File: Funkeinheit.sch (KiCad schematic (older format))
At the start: 41 parts, among them Q3 MMBT5551-TP, Q4 MMBT5551-TP, Q5 MMBT5551-TP, Q6 MMBT5551-TP, Q7 MMBT5551-TP, Q8 MMBT5551-TP, U4 LTC3113, U5 RFM23BP

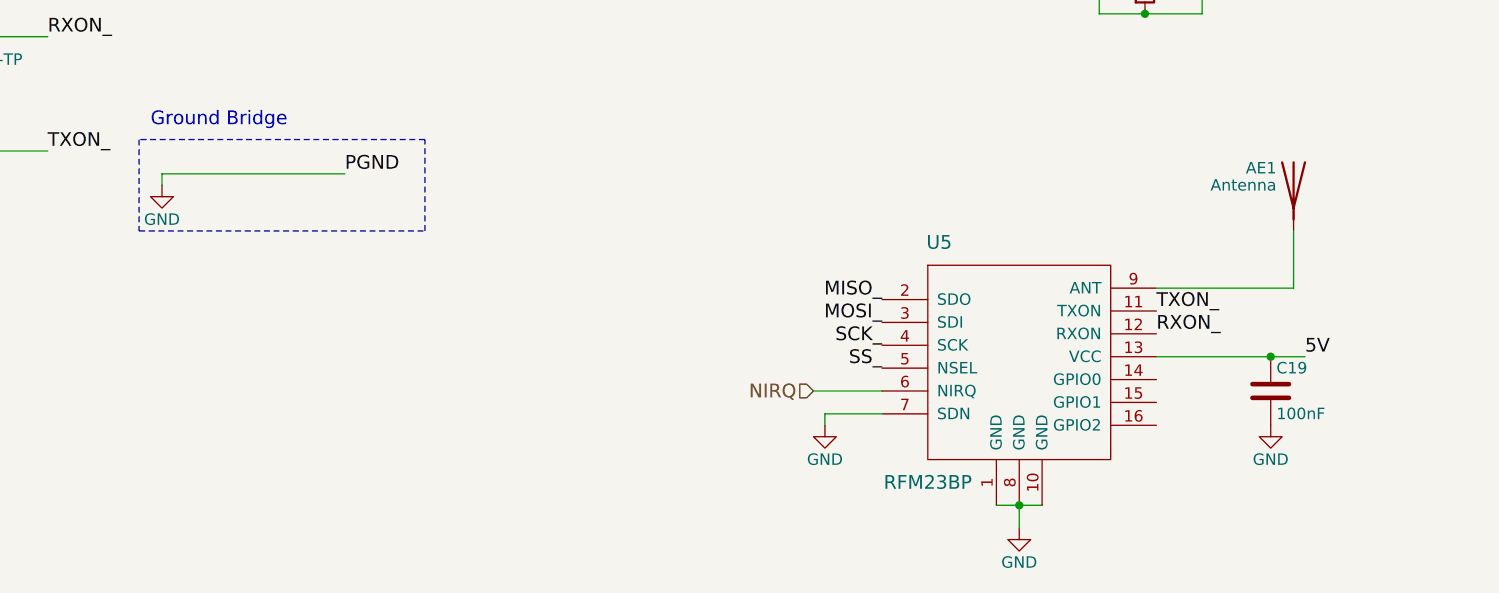
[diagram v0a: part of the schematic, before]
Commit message: Adds RFM23BP Footprint and places module on board
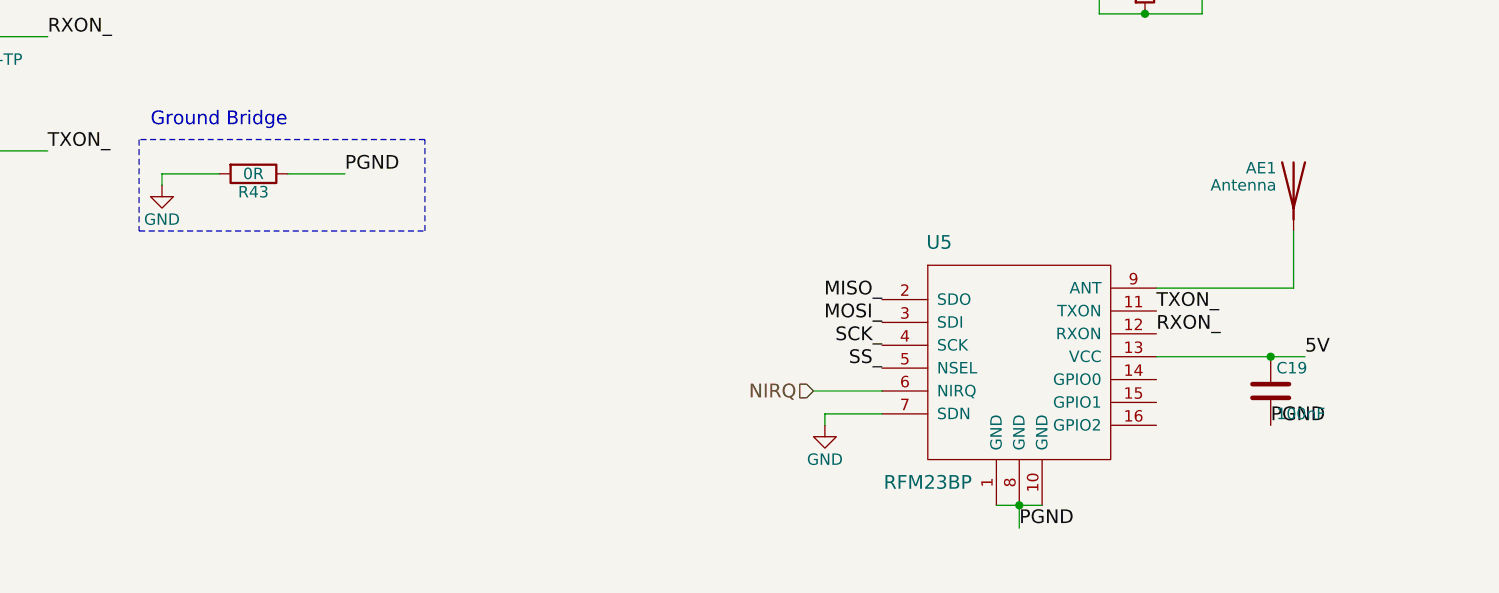
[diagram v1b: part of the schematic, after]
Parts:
- added R43: 0R, Resistors_SMD:R_0603_HandSoldering, symbol R
- C16: footprint Capacitors_SMD:C_1210_HandSoldering -> Capacitors_SMD:C_0603_HandSoldering
- U5: footprint (none) -> HopeRF:RFM23BP
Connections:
- net GND: now also R43.2; no longer C13.2, C14.2, C15.2, C19.2, U4.1 (PGND), U4.10 (PGND), U4.11 (PGND), U4.20 (PGND), U4.21 (PAD), U5.1 (GND), U5.10 (GND), U5.8 (GND)
- new net PGND: C13.2, C14.2, C15.2, C19.2, R43.1, U4.1 (PGND), U4.10 (PGND), U4.11 (PGND), U4.20 (PGND), U4.21 (PAD), U5.1 (GND), U5.10 (GND), U5.8 (GND)
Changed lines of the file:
@@
 Wire Wire Line
 	4750 3700 4750 3650
-Wire Wire Line
-	4750 3650 5550 3650
 Text Label 5550 3650 0    60   ~ 0
 PGND
@@
 F 0 "C16" H 9075 2200 50  0000 L CNN
 F 1 "47pF" H 9075 2000 50  0000 L CNN
-F 2 "Capacitors_SMD:C_1210_HandSoldering" H 9088 1950 50  0001 C CNN
+F 2 "Capacitors_SMD:C_0603_HandSoldering" H 9088 1950 50  0001 C CNN
 F 3 "" H 9050 2100 50  0001 C CNN
 	1    9050 2100
@@
 F 0 "U5" H 8150 5050 60  0000 C CNN
 F 1 "RFM23BP" H 8100 4000 60  0000 C CNN
-F 2 "" H 9000 3800 60  0001 C CNN
+F 2 "HopeRF:RFM23BP" H 9000 3800 60  0001 C CNN
 F 3 "" H 9000 3800 60  0001 C CNN
 	1    8500 4500
@@
 Wire Wire Line
 	9700 4150 9700 3900
-$Comp
-L GND #PWR035
-U 1 1 59C98D82
-P 8500 5200
-F 0 "#PWR035" H 8500 4950 50  0001 C CNN
-F 1 "GND" H 8500 5050 50  0000 C CNN
-F 2 "" H 8500 5200 50  0001 C CNN
-F 3 "" H 8500 5200 50  0001 C CNN
-	1    8500 5200
-	1    0    0    -1
-$EndComp
 Wire Wire Line
 	8400 5100 8600 5100
@@
 Connection ~ 8500 5100
 $Comp
-L GND #PWR036
+L GND #PWR035
 U 1 1 59C9947D
 P 7650 4750
-F 0 "#PWR036" H 7650 4500 50  0001 C CNN
+F 0 "#PWR035" H 7650 4500 50  0001 C CNN
 F 1 "GND" H 7650 4600 50  0000 C CNN
 F 2 "" H 7650 4750 50  0001 C CNN
@@
 F 3 "" H 9600 4600 50  0001 C CNN
 	1    9600 4600
-	1    0    0    -1
-$EndComp
-$Comp
-L GND #PWR037
-U 1 1 59CB2BA8
-P 9600 4750
-F 0 "#PWR037" H 9600 4500 50  0001 C CNN
-F 1 "GND" H 9600 4600 50  0000 C CNN
-F 2 "" H 9600 4750 50  0001 C CNN
-F 3 "" H 9600 4750 50  0001 C CNN
-	1    9600 4750
 	1    0    0    -1
 $EndComp
@@
 Text Label 9100 4350 0    60   ~ 0
 RXON_
+$Comp
+L R R43
+U 1 1 59DBF7EA
+P 5150 3650
+F 0 "R43" V 5230 3650 50  0000 C CNN
+F 1 "0R" V 5150 3650 50  0000 C CNN
+F 2 "Resistors_SMD:R_0603_HandSoldering" V 5080 3650 50  0001 C CNN
+F 3 "" H 5150 3650 50  0001 C CNN
+	1    5150 3650
+	0    1    1    0
+$EndComp
+Wire Wire Line
+	4750 3650 5000 3650
+Wire Wire Line
+	5300 3650 5550 3650
+Text Label 8500 5200 0    60   ~ 0
+PGND
+Text Label 9600 4750 0    60   ~ 0
+PGND
 $EndSCHEMATC

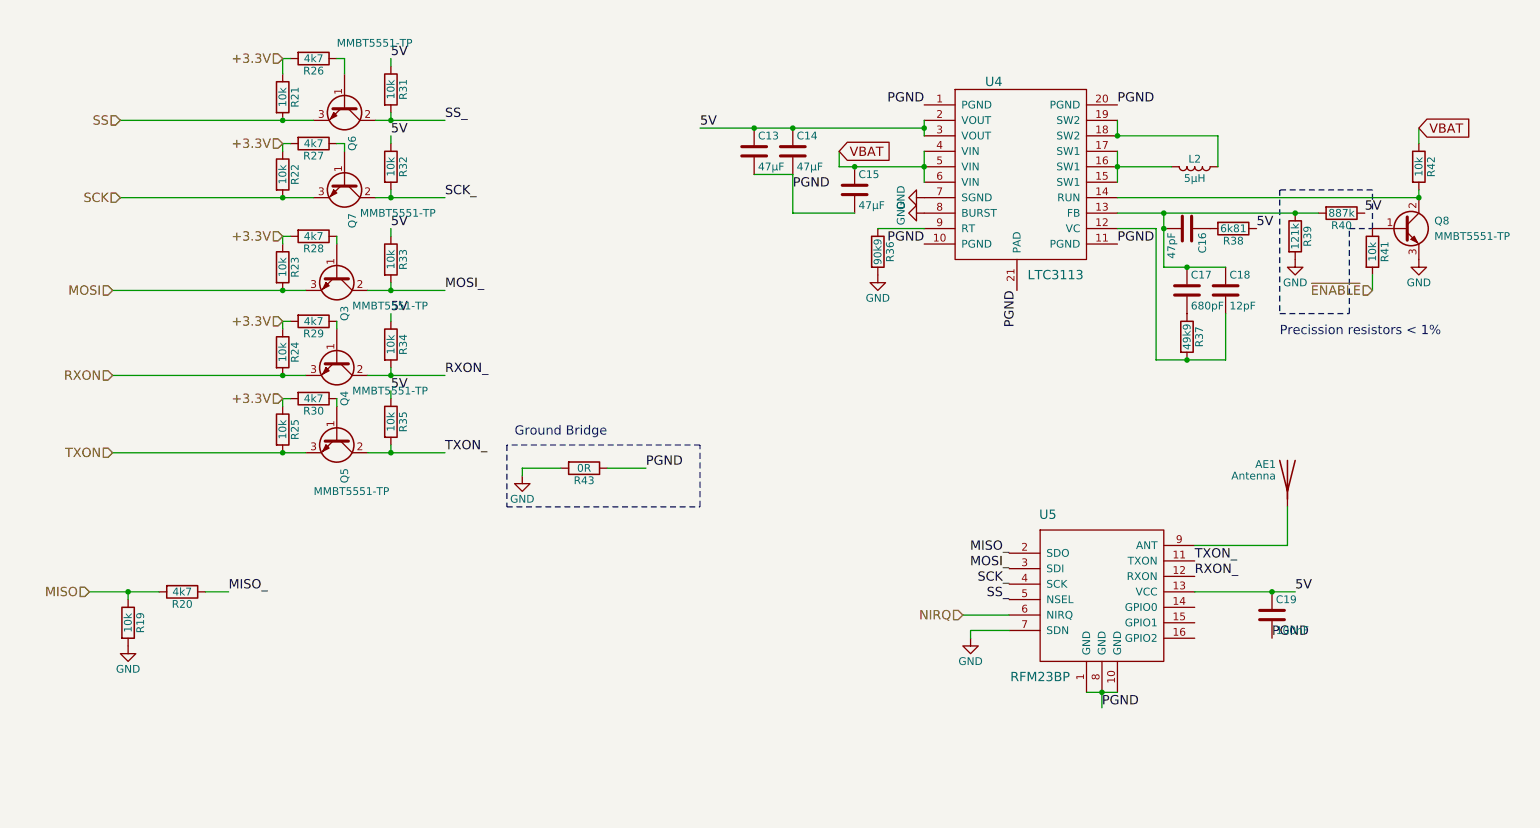
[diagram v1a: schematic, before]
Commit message: Adds Levelshifter for NIRQ
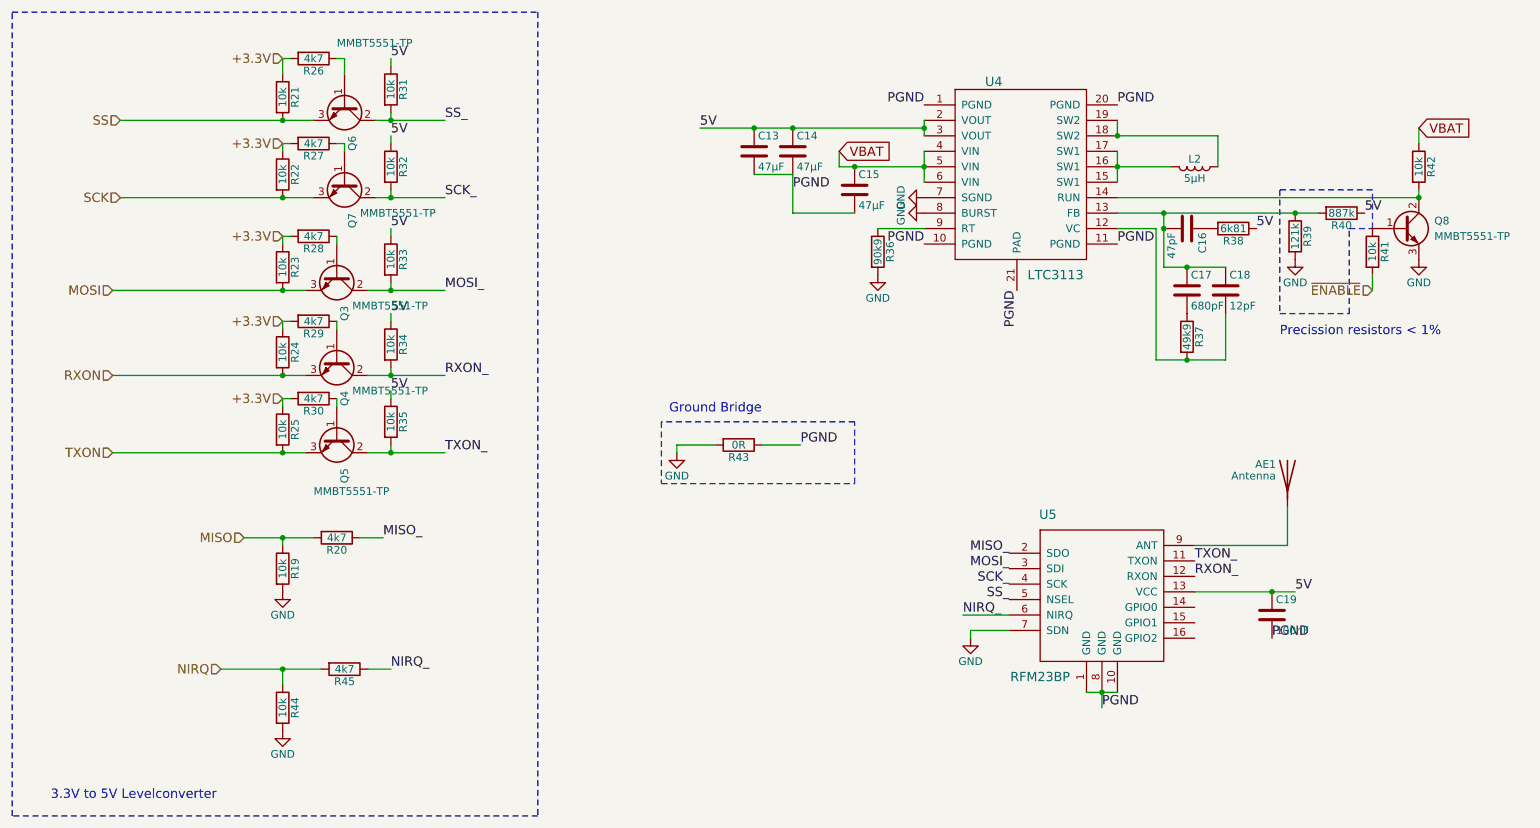
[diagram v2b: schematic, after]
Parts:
- added R44: 10k, Resistors_SMD:R_0603_HandSoldering, symbol R
- added R45: 4k7, Resistors_SMD:R_0603_HandSoldering, symbol R
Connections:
- net GND: now also R44.2
- net NIRQ: now also R44.1, R45.2; no longer U5.6 (NIRQ)
- new net NIRQ_: R45.1, U5.6 (NIRQ)
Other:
- note added: "3.3V to 5V Levelconverter"
- moved on the sheet: R19, R20, R43
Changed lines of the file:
@@
 L R R19
 U 1 1 5994BD7C
-P 2200 4650
-F 0 "R19" V 2280 4650 50  0000 C CNN
-F 1 "10k" V 2200 4650 50  0000 C CNN
-F 2 "Resistors_SMD:R_0603_HandSoldering" V 2130 4650 50  0001 C CNN
-F 3 "" H 2200 4650 50  0001 C CNN
-	1    2200 4650
+P 3200 4300
+F 0 "R19" V 3280 4300 50  0000 C CNN
+F 1 "10k" V 3200 4300 50  0000 C CNN
+F 2 "Resistors_SMD:R_0603_HandSoldering" V 3130 4300 50  0001 C CNN
+F 3 "" H 3200 4300 50  0001 C CNN
+	1    3200 4300
 	1    0    0    -1
 $EndComp
@@
 L R R20
 U 1 1 5994BD83
-P 2550 4450
-F 0 "R20" V 2630 4450 50  0000 C CNN
-F 1 "4k7" V 2550 4450 50  0000 C CNN
-F 2 "Resistors_SMD:R_0603_HandSoldering" V 2480 4450 50  0001 C CNN
-F 3 "" H 2550 4450 50  0001 C CNN
-	1    2550 4450
-	0    1    1    0
-$EndComp
-Text Label 2850 4450 0    60   ~ 0
+P 3550 4100
+F 0 "R20" V 3630 4100 50  0000 C CNN
+F 1 "4k7" V 3550 4100 50  0000 C CNN
+F 2 "Resistors_SMD:R_0603_HandSoldering" V 3480 4100 50  0001 C CNN
+F 3 "" H 3550 4100 50  0001 C CNN
+	1    3550 4100
+	0    1    1    0
+$EndComp
+Text Label 3850 4100 0    60   ~ 0
 MISO_
 Text HLabel 2150 1400 0    60   Input ~ 0
@@
 Text HLabel 2100 2500 0    60   Input ~ 0
 MOSI
-Text HLabel 1950 4450 0    60   Input ~ 0
+Text HLabel 2950 4100 0    60   Input ~ 0
 MISO
 Text Label 4250 3050 0    60   ~ 0
@@
 	3750 3050 4250 3050
 Wire Wire Line
-	2700 4450 2850 4450
-Connection ~ 2200 4450
-Wire Wire Line
-	2200 4500 2200 4450
-Wire Wire Line
-	1950 4450 2400 4450
+	3700 4100 3850 4100
+Connection ~ 3200 4100
+Wire Wire Line
+	3200 4150 3200 4100
+Wire Wire Line
+	2950 4100 3400 4100
 Wire Wire Line
 	3750 2500 4250 2500
@@
 	3800 1400 4250 1400
 $Comp
-L GND #PWR028
+L GND #PWR28
 U 1 1 59B87665
-P 2200 4800
-F 0 "#PWR028" H 2200 4550 50  0001 C CNN
-F 1 "GND" H 2200 4650 50  0000 C CNN
-F 2 "" H 2200 4800 50  0001 C CNN
-F 3 "" H 2200 4800 50  0001 C CNN
-	1    2200 4800
-	1    0    0    -1
-$EndComp
-$Comp
-L GND #PWR029
+P 3200 4450
+F 0 "#PWR28" H 3200 4200 50  0001 C CNN
+F 1 "GND" H 3200 4300 50  0000 C CNN
+F 2 "" H 3200 4450 50  0001 C CNN
+F 3 "" H 3200 4450 50  0001 C CNN
+	1    3200 4450
+	1    0    0    -1
+$EndComp
+$Comp
+L GND #PWR30
 U 1 1 59B89289
-P 4750 3700
-F 0 "#PWR029" H 4750 3450 50  0001 C CNN
-F 1 "GND" H 4750 3550 50  0000 C CNN
-F 2 "" H 4750 3700 50  0001 C CNN
-F 3 "" H 4750 3700 50  0001 C CNN
-	1    4750 3700
-	1    0    0    -1
-$EndComp
-Wire Wire Line
-	4750 3700 4750 3650
-Text Label 5550 3650 0    60   ~ 0
+P 5750 3550
+F 0 "#PWR30" H 5750 3300 50  0001 C CNN
+F 1 "GND" H 5750 3400 50  0000 C CNN
+F 2 "" H 5750 3550 50  0001 C CNN
+F 3 "" H 5750 3550 50  0001 C CNN
+	1    5750 3550
+	1    0    0    -1
+$EndComp
+Wire Wire Line
+	5750 3550 5750 3500
+Text Label 6550 3500 0    60   ~ 0
 PGND
 Wire Notes Line
-	4650 3500 4650 3900
-Wire Notes Line
-	4650 3900 5900 3900
-Wire Notes Line
-	5900 3900 5900 3500
-Wire Notes Line
-	5900 3500 4650 3500
-Text Notes 4700 3450 0    60   ~ 0
+	5650 3350 5650 3750
+Wire Notes Line
+	5650 3750 6900 3750
+Wire Notes Line
+	6900 3750 6900 3350
+Wire Notes Line
+	6900 3350 5650 3350
+Text Notes 5700 3300 0    60   ~ 0
 Ground Bridge
 Text Label 7350 1300 2    60   ~ 0
@@
 PGND
 $Comp
-L GND #PWR030
+L GND #PWR32
 U 1 1 59BD80CC
 P 7350 1900
-F 0 "#PWR030" H 7350 1650 50  0001 C CNN
+F 0 "#PWR32" H 7350 1650 50  0001 C CNN
 F 1 "GND" H 7350 1750 50  0000 C CNN
 F 2 "" H 7350 1900 50  0001 C CNN
@@
 5V
 $Comp
-L GND #PWR031
+L GND #PWR33
 U 1 1 59C59DAC
 P 7350 2000
-F 0 "#PWR031" H 7350 1750 50  0001 C CNN
+F 0 "#PWR33" H 7350 1750 50  0001 C CNN
 F 1 "GND" H 7350 1850 50  0000 C CNN
 F 2 "" H 7350 2000 50  0001 C CNN
@@
 	10550 1850 10550 1900
 $Comp
-L GND #PWR032
+L GND #PWR36
 U 1 1 59C5A346
 P 10550 2300
-F 0 "#PWR032" H 10550 2050 50  0001 C CNN
+F 0 "#PWR36" H 10550 2050 50  0001 C CNN
 F 1 "GND" H 10550 2150 50  0000 C CNN
 F 2 "" H 10550 2300 50  0001 C CNN
@@
 $EndComp
 $Comp
-L GND #PWR033
+L GND #PWR31
 U 1 1 59C5FB2A
 P 7050 2400
-F 0 "#PWR033" H 7050 2150 50  0001 C CNN
+F 0 "#PWR31" H 7050 2150 50  0001 C CNN
 F 1 "GND" H 7050 2250 50  0000 C CNN
 F 2 "" H 7050 2400 50  0001 C CNN
@@
 $EndComp
 $Comp
-L GND #PWR034
+L GND #PWR35
 U 1 1 59C6029F
 P 9750 2300
-F 0 "#PWR034" H 9750 2050 50  0001 C CNN
+F 0 "#PWR35" H 9750 2050 50  0001 C CNN
 F 1 "GND" H 9750 2150 50  0000 C CNN
 F 2 "" H 9750 2300 50  0001 C CNN
@@
 Connection ~ 8500 5100
 $Comp
-L GND #PWR035
+L GND #PWR34
 U 1 1 59C9947D
 P 7650 4750
-F 0 "#PWR035" H 7650 4500 50  0001 C CNN
+F 0 "#PWR34" H 7650 4500 50  0001 C CNN
 F 1 "GND" H 7650 4600 50  0000 C CNN
 F 2 "" H 7650 4750 50  0001 C CNN
@@
 Wire Wire Line
 	7900 4600 7600 4600
-Text HLabel 7600 4600 0    60   Input ~ 0
-NIRQ
 Wire Wire Line
 	9100 4450 9750 4450
@@
 L R R43
 U 1 1 59DBF7EA
-P 5150 3650
-F 0 "R43" V 5230 3650 50  0000 C CNN
-F 1 "0R" V 5150 3650 50  0000 C CNN
-F 2 "Resistors_SMD:R_0603_HandSoldering" V 5080 3650 50  0001 C CNN
-F 3 "" H 5150 3650 50  0001 C CNN
-	1    5150 3650
-	0    1    1    0
-$EndComp
-Wire Wire Line
-	4750 3650 5000 3650
-Wire Wire Line
-	5300 3650 5550 3650
+P 6150 3500
+F 0 "R43" V 6230 3500 50  0000 C CNN
+F 1 "0R" V 6150 3500 50  0000 C CNN
+F 2 "Resistors_SMD:R_0603_HandSoldering" V 6080 3500 50  0001 C CNN
+F 3 "" H 6150 3500 50  0001 C CNN
+	1    6150 3500
+	0    1    1    0
+$EndComp
+Wire Wire Line
+	5750 3500 6000 3500
+Wire Wire Line
+	6300 3500 6550 3500
 Text Label 8500 5200 0    60   ~ 0
 PGND
 Text Label 9600 4750 0    60   ~ 0
 PGND
+$Comp
+L R R45
+U 1 1 59DE3235
+P 3600 4950
+F 0 "R45" V 3680 4950 50  0000 C CNN
+F 1 "4k7" V 3600 4950 50  0000 C CNN
+F 2 "Resistors_SMD:R_0603_HandSoldering" V 3530 4950 50  0001 C CNN
+F 3 "" H 3600 4950 50  0001 C CNN
+	1    3600 4950
+	0    1    1    0
+$EndComp
+$Comp
+L R R44
+U 1 1 59DE32B8
+P 3200 5200
+F 0 "R44" V 3280 5200 50  0000 C CNN
+F 1 "10k" V 3200 5200 50  0000 C CNN
+F 2 "Resistors_SMD:R_0603_HandSoldering" V 3130 5200 50  0001 C CNN
+F 3 "" H 3200 5200 50  0001 C CNN
+	1    3200 5200
+	1    0    0    -1
+$EndComp
+$Comp
+L GND #PWR29
+U 1 1 59DE335D
+P 3200 5350
+F 0 "#PWR29" H 3200 5100 50  0001 C CNN
+F 1 "GND" H 3200 5200 50  0000 C CNN
+F 2 "" H 3200 5350 50  0001 C CNN
+F 3 "" H 3200 5350 50  0001 C CNN
+	1    3200 5350
+	1    0    0    -1
+$EndComp
+Wire Wire Line
+	3200 5050 3200 4950
+Wire Wire Line
+	2800 4950 3450 4950
+Wire Wire Line
+	3750 4950 3900 4950
+Connection ~ 3200 4950
+Text HLabel 2800 4950 0    60   Input ~ 0
+NIRQ
+Text Label 7600 4600 0    60   ~ 0
+NIRQ_
+Text Label 3900 4950 0    60   ~ 0
+NIRQ_
+Wire Notes Line
+	1450 700  4850 700
+Wire Notes Line
+	4850 700  4850 5900
+Wire Notes Line
+	4850 5900 1450 5900
+Wire Notes Line
+	1450 5900 1450 700
+Text Notes 1700 5800 0    60   ~ 0
+3.3V to 5V Levelconverter
 $EndSCHEMATC

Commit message: Layout Module1 prefinish
Modules Placed
Ground Plane placed
Supply Plane placed
TODO: Add cubesat connector, Place Antenna connector, Place burnwire connector, Review
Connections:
- net GND: no longer U5.7 (SDN)
- net PGND: now also U5.7 (SDN)
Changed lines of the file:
@@
 LIBS:contrib
 LIBS:valves
-LIBS:nxp-ic
-LIBS:7400-ic
 LIBS:cubesatFunkmodul-cache
 LIBS:funkmodul
-LIBS:DISCO_Connector
 EELAYER 25 0
 EELAYER END
@@
 	3800 1400 4250 1400
 $Comp
-L GND #PWR28
+L GND #PWR027
 U 1 1 59B87665
 P 3200 4450
-F 0 "#PWR28" H 3200 4200 50  0001 C CNN
+F 0 "#PWR027" H 3200 4200 50  0001 C CNN
 F 1 "GND" H 3200 4300 50  0000 C CNN
 F 2 "" H 3200 4450 50  0001 C CNN
@@
 $EndComp
 $Comp
-L GND #PWR30
+L GND #PWR028
 U 1 1 59B89289
 P 5750 3550
-F 0 "#PWR30" H 5750 3300 50  0001 C CNN
+F 0 "#PWR028" H 5750 3300 50  0001 C CNN
 F 1 "GND" H 5750 3400 50  0000 C CNN
 F 2 "" H 5750 3550 50  0001 C CNN
@@
 PGND
 $Comp
-L GND #PWR32
+L GND #PWR029
 U 1 1 59BD80CC
 P 7350 1900
-F 0 "#PWR32" H 7350 1650 50  0001 C CNN
+F 0 "#PWR029" H 7350 1650 50  0001 C CNN
 F 1 "GND" H 7350 1750 50  0000 C CNN
 F 2 "" H 7350 1900 50  0001 C CNN
@@
 5V
 $Comp
-L GND #PWR33
+L GND #PWR030
 U 1 1 59C59DAC
 P 7350 2000
-F 0 "#PWR33" H 7350 1750 50  0001 C CNN
+F 0 "#PWR030" H 7350 1750 50  0001 C CNN
 F 1 "GND" H 7350 1850 50  0000 C CNN
 F 2 "" H 7350 2000 50  0001 C CNN
@@
 	10550 1850 10550 1900
 $Comp
-L GND #PWR36
+L GND #PWR031
 U 1 1 59C5A346
 P 10550 2300
-F 0 "#PWR36" H 10550 2050 50  0001 C CNN
+F 0 "#PWR031" H 10550 2050 50  0001 C CNN
 F 1 "GND" H 10550 2150 50  0000 C CNN
 F 2 "" H 10550 2300 50  0001 C CNN
@@
 $EndComp
 $Comp
-L GND #PWR31
+L GND #PWR032
 U 1 1 59C5FB2A
 P 7050 2400
-F 0 "#PWR31" H 7050 2150 50  0001 C CNN
+F 0 "#PWR032" H 7050 2150 50  0001 C CNN
 F 1 "GND" H 7050 2250 50  0000 C CNN
 F 2 "" H 7050 2400 50  0001 C CNN
@@
 $EndComp
 $Comp
-L GND #PWR35
+L GND #PWR033
 U 1 1 59C6029F
 P 9750 2300
-F 0 "#PWR35" H 9750 2050 50  0001 C CNN
+F 0 "#PWR033" H 9750 2050 50  0001 C CNN
 F 1 "GND" H 9750 2150 50  0000 C CNN
 F 2 "" H 9750 2300 50  0001 C CNN
@@
 	9700 4150 9700 3900
 Wire Wire Line
-	8400 5100 8600 5100
+	7650 5100 8600 5100
 Wire Wire Line
 	8500 5100 8500 5200
 Connection ~ 8500 5100
-$Comp
-L GND #PWR34
-U 1 1 59C9947D
-P 7650 4750
-F 0 "#PWR34" H 7650 4500 50  0001 C CNN
-F 1 "GND" H 7650 4600 50  0000 C CNN
-F 2 "" H 7650 4750 50  0001 C CNN
-F 3 "" H 7650 4750 50  0001 C CNN
-	1    7650 4750
-	1    0    0    -1
-$EndComp
 Wire Wire Line
 	7900 4700 7650 4700
 Wire Wire Line
-	7650 4700 7650 4750
+	7650 4700 7650 5100
 Wire Wire Line
 	7900 4600 7600 4600
@@
 $EndComp
 $Comp
-L GND #PWR29
+L GND #PWR034
 U 1 1 59DE335D
 P 3200 5350
-F 0 "#PWR29" H 3200 5100 50  0001 C CNN
+F 0 "#PWR034" H 3200 5100 50  0001 C CNN
 F 1 "GND" H 3200 5200 50  0000 C CNN
 F 2 "" H 3200 5350 50  0001 C CNN
@@
 Text Notes 1700 5800 0    60   ~ 0
 3.3V to 5V Levelconverter
+Connection ~ 8400 5100
 $EndSCHEMATC
